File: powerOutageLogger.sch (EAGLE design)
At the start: 31 parts, among them J1 2.1MMJACKTHM, U1 ATmega328P, U2 78L05, Y1 16MHz

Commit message: v1.1
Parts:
- added C10: 100nF, _jc:C-US025-025X050
- C7: value 27pF -> 100nF
- C9: value 100nF -> 27pF
- S1, S2: device _jc:10-XXOCT -> _jc:B3F-312X
- S3: value DOWN -> DN; device _jc:10-XXOCT -> _jc:B3F-312X
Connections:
- removed net PD4: JP2.3, U1.PD4(XCK/T0)
- removed net PD5: S2.S, S2.S1, U1.PD5(T1)
- removed net PD6: S1.S, S1.S1, U1.PD6(AIN0)
- net /RESET: now also C10.1; no longer C9.1
- net GND: now also C9.2, S1.P$1, S2.P$1, S3.P$1; no longer S1.P, S1.P1, S2.P, S2.P1, S3.P, S3.P1
- net MOSI: now also S1.P$2
- net N$9: now also C7.1; no longer C5.1
- net PC3: now also PCB2.E; no longer PCB2.RS
- net PD2: now also PCB2.RS; no longer PCB2.E
- net PD3: now also JP2.3
- net PD7: now also S3.P$2; no longer S3.S, S3.S1
- net RST: now also C10.2; no longer C9.2
- net SS: now also S2.P$2
- net VCC: now also C5.1
- net XTAL1: now also C9.1; no longer C8.1
- net XTAL2: now also C8.1; no longer C7.1
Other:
- note added: "1.1"
- note removed: "1.0"
- moved on the sheet: C5, C7, C8, C9

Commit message: v1.1
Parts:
- added R5: 0, _jc:R-US_0204/6
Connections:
- new net N$6: PCB2.A, R5.2
- net PB1: now also R5.1; no longer PCB2.A
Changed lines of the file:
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@@
 <part name="S3" library="_jc" deviceset="B3F-312X" device="" value="DN"/>
 <part name="C5" library="_jc" deviceset="C-US" device="025-025X050" value="100nF"/>
+<part name="R5" library="_jc" deviceset="R-US_" device="0204/6" value="0"/>
 </parts>
 <sheets>
@@
 <instance part="S3" gate="G$1" x="231.14" y="152.4" rot="R90"/>
 <instance part="C5" gate="G$1" x="218.44" y="66.04"/>
+<instance part="R5" gate="G$1" x="142.24" y="177.8" smashed="yes" rot="R180">
+<attribute name="NAME" x="138.2014" y="181.61" size="1.778" layer="95"/>
+<attribute name="VALUE" x="143.002" y="181.61" size="1.778" layer="96"/>
+</instance>
 </instances>
 <busses>
@@
 </segment>
 <segment>
-<pinref part="PCB2" gate="G$1" pin="A"/>
-<wire x1="132.08" y1="172.72" x2="142.24" y2="172.72" width="0.1524" layer="91"/>
-<label x="137.16" y="172.72" size="1.778" layer="95"/>
+<pinref part="R5" gate="G$1" pin="1"/>
+<wire x1="147.32" y1="177.8" x2="154.94" y2="177.8" width="0.1524" layer="91"/>
+<label x="149.86" y="177.8" size="1.778" layer="95"/>
 </segment>
 </net>
@@
 </segment>
 </net>
+<net name="N$6" class="0">
+<segment>
+<pinref part="PCB2" gate="G$1" pin="A"/>
+<wire x1="132.08" y1="172.72" x2="134.62" y2="172.72" width="0.1524" layer="91"/>
+<wire x1="134.62" y1="172.72" x2="134.62" y2="177.8" width="0.1524" layer="91"/>
+<pinref part="R5" gate="G$1" pin="2"/>
+<wire x1="134.62" y1="177.8" x2="137.16" y2="177.8" width="0.1524" layer="91"/>
+</segment>
+</net>

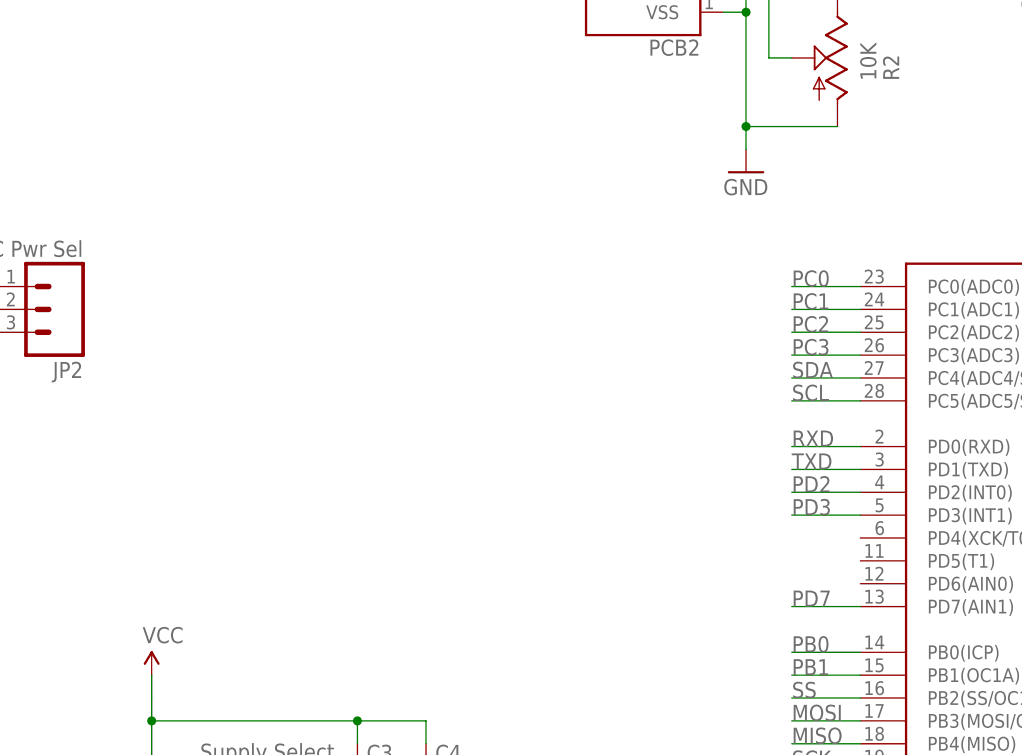
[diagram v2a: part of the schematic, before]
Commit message: Version 1.1 Added ReadMe.txt Added schematic.png
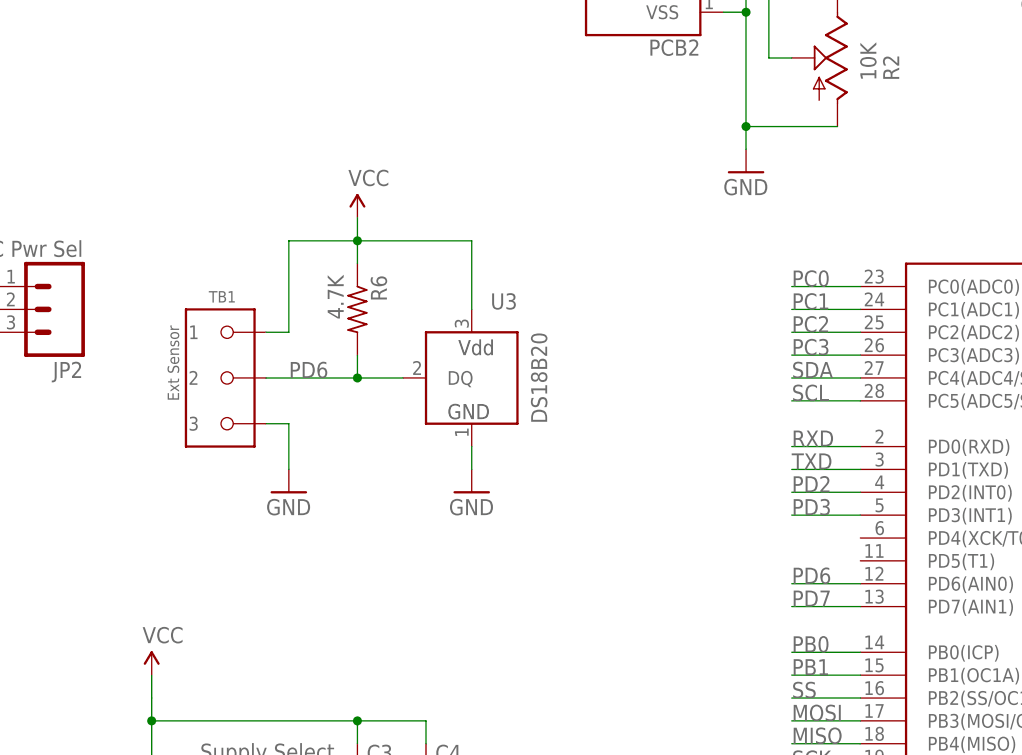
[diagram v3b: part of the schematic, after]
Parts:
- added R6: 4.7K, _jc:R-US_0204/6
- added TB1: Ext Sensor, _jc:OST-TB-33.5MM
- added U3: DS18B20, _jc:DS18B20
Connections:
- new net PD6: R6.2, TB1.2, U1.PD6(AIN0), U3.DQ
- net GND: now also TB1.3, U3.GND
- net VCC: now also R6.1, TB1.1, U3.VDD
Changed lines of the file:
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@@
 <layer number="109" name="fp9" color="7" fill="1" visible="no" active="yes"/>
 <layer number="110" name="fp0" color="7" fill="1" visible="no" active="yes"/>
+<layer number="111" name="LPC17xx" color="7" fill="1" visible="yes" active="yes"/>
+<layer number="112" name="tSilk" color="7" fill="1" visible="yes" active="yes"/>
 <layer number="116" name="Patch_BOT" color="9" fill="4" visible="yes" active="yes"/>
 <layer number="121" name="_tsilk" color="7" fill="1" visible="yes" active="yes"/>
@@
 <layer number="123" name="tTestmark" color="7" fill="1" visible="no" active="yes"/>
 <layer number="124" name="bTestmark" color="7" fill="1" visible="no" active="yes"/>
+<layer number="125" name="_tNames" color="7" fill="1" visible="yes" active="yes"/>
+<layer number="126" name="_bNames" color="7" fill="1" visible="yes" active="yes"/>
+<layer number="127" name="_tValues" color="7" fill="1" visible="yes" active="yes"/>
+<layer number="128" name="_bValues" color="7" fill="1" visible="yes" active="yes"/>
 <layer number="131" name="tAdjust" color="7" fill="1" visible="no" active="yes"/>
 <layer number="132" name="bAdjust" color="7" fill="1" visible="no" active="yes"/>
 <layer number="144" name="Drill_legend" color="7" fill="1" visible="yes" active="yes"/>
 <layer number="151" name="HeatSink" color="7" fill="1" visible="yes" active="yes"/>
+<layer number="152" name="_bDocu" color="7" fill="1" visible="yes" active="yes"/>
 <layer number="199" name="Contour" color="7" fill="1" visible="yes" active="yes"/>
 <layer number="200" name="200bmp" color="1" fill="10" visible="yes" active="yes"/>
@@
 <layer number="215" name="215bmp" color="7" fill="1" visible="no" active="yes"/>
 <layer number="216" name="216bmp" color="7" fill="1" visible="no" active="yes"/>
+<layer number="217" name="217bmp" color="7" fill="1" visible="yes" active="yes"/>
+<layer number="218" name="218bmp" color="7" fill="1" visible="yes" active="yes"/>
+<layer number="219" name="219bmp" color="7" fill="1" visible="yes" active="yes"/>
+<layer number="220" name="220bmp" color="7" fill="1" visible="yes" active="yes"/>
+<layer number="221" name="221bmp" color="7" fill="1" visible="yes" active="yes"/>
+<layer number="222" name="222bmp" color="7" fill="1" visible="yes" active="yes"/>
+<layer number="223" name="223bmp" color="7" fill="1" visible="yes" active="yes"/>
+<layer number="224" name="224bmp" color="7" fill="1" visible="yes" active="yes"/>
+<layer number="248" name="Housing" color="7" fill="1" visible="yes" active="yes"/>
+<layer number="249" name="Edge" color="7" fill="1" visible="yes" active="yes"/>
 <layer number="250" name="Descript" color="3" fill="1" visible="no" active="no"/>
 <layer number="251" name="SMDround" color="12" fill="11" visible="no" active="no"/>
@@
 <part name="C5" library="_jc" deviceset="C-US" device="025-025X050" value="100nF"/>
 <part name="R5" library="_jc" deviceset="R-US_" device="0204/6" value="0"/>
+<part name="U3" library="_jc" deviceset="DS18B20" device=""/>
+<part name="R6" library="_jc" deviceset="R-US_" device="0204/6" value="4.7K"/>
+<part name="P+8" library="SparkFun" deviceset="VCC" device=""/>
+<part name="GND16" library="supply1" deviceset="GND" device=""/>
+<part name="TB1" library="_jc" deviceset="OST-TB-3" device="3.5MM" value="Ext Sensor"/>
+<part name="GND17" library="supply1" deviceset="GND" device=""/>
 </parts>
 <sheets>
@@
 <attribute name="VALUE" x="143.002" y="181.61" size="1.778" layer="96"/>
 </instance>
+<instance part="U3" gate="G$1" x="104.14" y="96.52" smashed="yes" rot="MR0">
+<attribute name="NAME" x="109.22" y="104.14" size="1.778" layer="95" rot="MR0"/>
+</instance>
+<instance part="R6" gate="G$1" x="91.44" y="104.14" rot="R270"/>
+<instance part="P+8" gate="1" x="91.44" y="114.3"/>
+<instance part="GND16" gate="1" x="104.14" y="83.82" smashed="yes">
+<attribute name="VALUE" x="101.6" y="81.28" size="1.778" layer="96"/>
+</instance>
+<instance part="TB1" gate="G$1" x="76.2" y="96.52"/>
+<instance part="GND17" gate="1" x="83.82" y="83.82" smashed="yes">
+<attribute name="VALUE" x="81.28" y="81.28" size="1.778" layer="96"/>
+</instance>
 </instances>
 <busses>
@@
 <pinref part="R4" gate="G$1" pin="2"/>
 <pinref part="P+7" gate="1" pin="VCC"/>
+</segment>
+<segment>
+<wire x1="104.14" y1="104.14" x2="104.14" y2="111.76" width="0.1524" layer="91"/>
+<wire x1="104.14" y1="111.76" x2="91.44" y2="111.76" width="0.1524" layer="91"/>
+<wire x1="91.44" y1="109.22" x2="91.44" y2="111.76" width="0.1524" layer="91"/>
+<wire x1="91.44" y1="111.76" x2="91.44" y2="114.3" width="0.1524" layer="91"/>
+<junction x="91.44" y="111.76"/>
+<pinref part="U3" gate="G$1" pin="VDD"/>
+<pinref part="R6" gate="G$1" pin="1"/>
+<pinref part="P+8" gate="1" pin="VCC"/>
+<wire x1="83.82" y1="101.6" x2="83.82" y2="111.76" width="0.1524" layer="91"/>
+<wire x1="83.82" y1="111.76" x2="91.44" y2="111.76" width="0.1524" layer="91"/>
+<pinref part="TB1" gate="G$1" pin="1"/>
+<wire x1="81.28" y1="101.6" x2="83.82" y2="101.6" width="0.1524" layer="91"/>
 </segment>
 </net>
@@
 <junction x="93.98" y="45.72"/>
 </segment>
+<segment>
+<wire x1="104.14" y1="88.9" x2="104.14" y2="86.36" width="0.1524" layer="91"/>
+<pinref part="U3" gate="G$1" pin="GND"/>
+<pinref part="GND16" gate="1" pin="GND"/>
+</segment>
+<segment>
+<pinref part="TB1" gate="G$1" pin="3"/>
+<pinref part="GND17" gate="1" pin="GND"/>
+<wire x1="81.28" y1="91.44" x2="83.82" y2="91.44" width="0.1524" layer="91"/>
+<wire x1="83.82" y1="91.44" x2="83.82" y2="86.36" width="0.1524" layer="91"/>
+</segment>
 </net>
 <net name="SCK" class="0">
@@
 </segment>
 </net>
+<net name="PD6" class="0">
+<segment>
+<pinref part="U3" gate="G$1" pin="DQ"/>
+<wire x1="96.52" y1="96.52" x2="91.44" y2="96.52" width="0.1524" layer="91"/>
+<pinref part="R6" gate="G$1" pin="2"/>
+<wire x1="91.44" y1="96.52" x2="81.28" y2="96.52" width="0.1524" layer="91"/>
+<wire x1="91.44" y1="99.06" x2="91.44" y2="96.52" width="0.1524" layer="91"/>
+<junction x="91.44" y="96.52"/>
+<label x="83.82" y="96.52" size="1.778" layer="95"/>
+<pinref part="TB1" gate="G$1" pin="2"/>
+</segment>
+<segment>
+<pinref part="U1" gate="G$1" pin="PD6(AIN0)"/>
+<wire x1="147.32" y1="73.66" x2="139.7" y2="73.66" width="0.1524" layer="91"/>
+<label x="139.7" y="73.66" size="1.778" layer="95"/>
+</segment>
+</net>
